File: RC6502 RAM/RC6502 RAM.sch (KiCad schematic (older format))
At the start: 23 parts, among them J3 RC6502_Backplane, U1 HM62256BLP-7, U2 74LS138, U3 74LS02, U4 74LS02, U5 74LS00

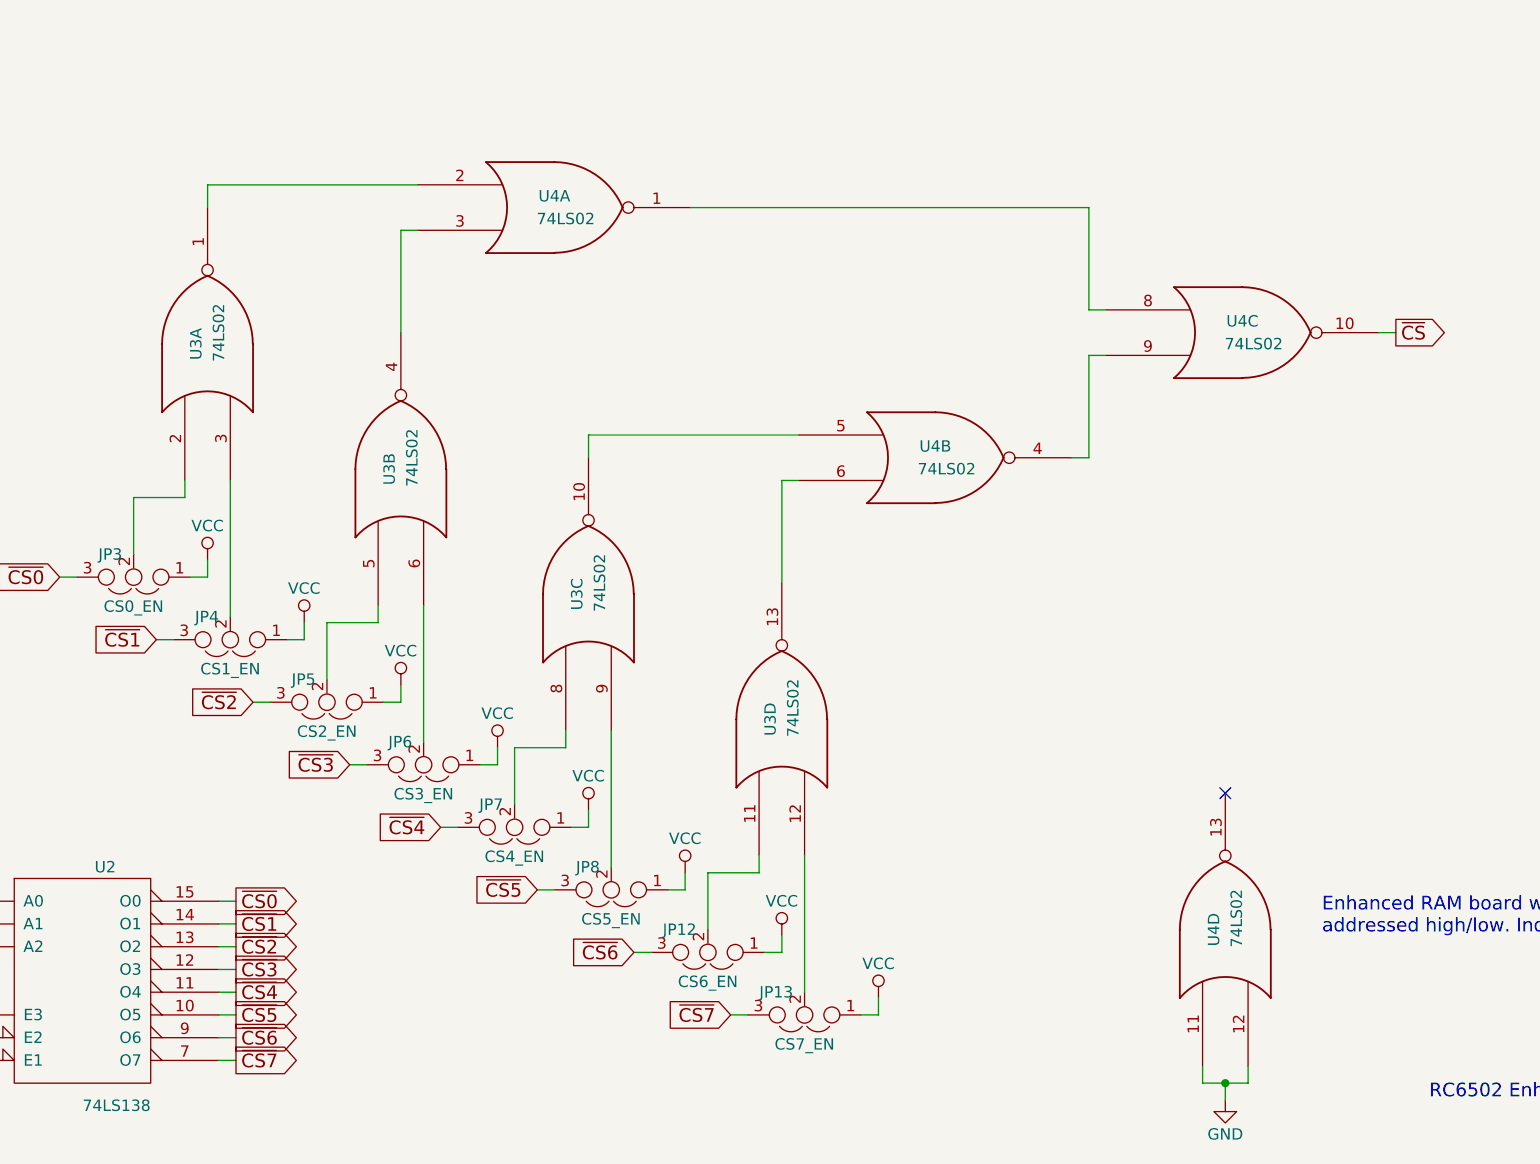
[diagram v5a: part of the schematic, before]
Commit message: Fixed RAM board block select logic
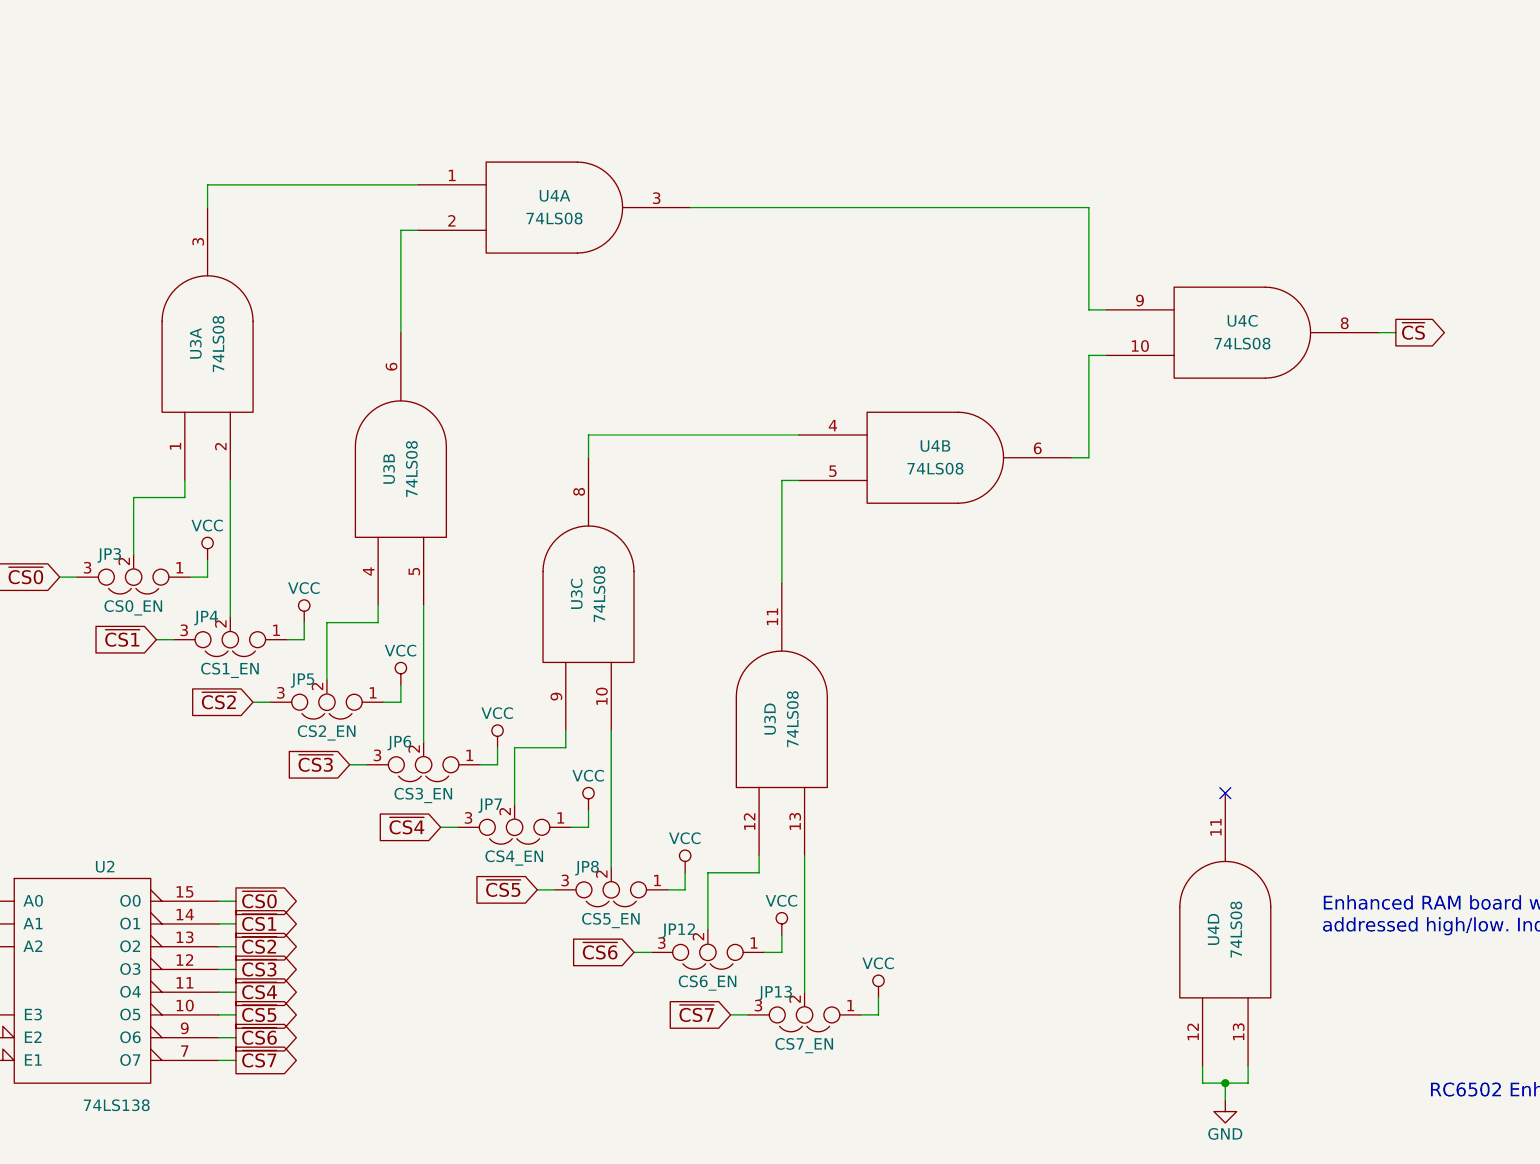
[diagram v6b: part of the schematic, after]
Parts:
- removed U3, U4: 74LS02, Housings_DIP:DIP-14_W7.62mm_Socket, symbol 74LS02
- added U3, U4: 74LS08, Housings_DIP:DIP-14_W7.62mm_Socket, symbol 74LS08
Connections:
- net GND: now also U3.7 (GND), U3.7 (GND), U3.7 (GND), U3.7 (GND), U4.12, U4.13, U4.7 (GND), U4.7 (GND), U4.7 (GND), U4.7 (GND)
- net VCC: now also U3.14 (VCC), U3.14 (VCC), U3.14 (VCC), U3.14 (VCC), U4.14 (VCC), U4.14 (VCC), U4.14 (VCC), U4.14 (VCC)
- net ~CS: now also U4.8
- net at JP3.2: now also U3.1
- net at JP4.2: now also U3.2
- net at JP5.2: now also U3.4
- net at JP6.2: now also U3.5
- net at JP7.2: now also U3.9
- net at JP8.2: now also U3.10
- net at JP12.2: now also U3.12
- net at JP13.2: now also U3.13
- new net: U3.3, U4.1
- new net: U3.6, U4.2
- new net: U3.8, U4.4
- new net: U3.11, U4.5
- new net: U4.3, U4.9
- new net: U4.10, U4.6
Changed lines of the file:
@@
 Wire Wire Line
 	2125 5125 2125 5200
-$Comp
-L 74LS02 U3
-U 1 1 5C1DAB94
-P 2125 4175
-F 0 "U3" H 2125 4225 50  0000 C CNN
-F 1 "74LS02" H 2175 4125 50  0000 C CNN
-F 2 "Housings_DIP:DIP-14_W7.62mm_Socket" H 2125 4175 50  0001 C CNN
-F 3 "" H 2125 4175 50  0001 C CNN
-	1    2125 4175
-	0    -1   -1   0
-$EndComp
 Wire Wire Line
 	1800 5100 1800 4850
@@
 Wire Wire Line
 	2975 5675 2975 5750
-$Comp
-L 74LS02 U3
-U 2 1 5C1DB812
-P 2975 4725
-F 0 "U3" H 2975 4775 50  0000 C CNN
-F 1 "74LS02" H 3025 4675 50  0000 C CNN
-F 2 "Housings_DIP:DIP-14_W7.62mm_Socket" H 2975 4725 50  0001 C CNN
-F 3 "" H 2975 4725 50  0001 C CNN
-	2    2975 4725
-	0    -1   -1   0
-$EndComp
 Wire Wire Line
 	2650 5650 2650 5400
@@
 Wire Wire Line
 	3800 6225 3800 6300
-$Comp
-L 74LS02 U3
-U 3 1 5C1DC564
-P 3800 5275
-F 0 "U3" H 3800 5325 50  0000 C CNN
-F 1 "74LS02" H 3850 5225 50  0000 C CNN
-F 2 "Housings_DIP:DIP-14_W7.62mm_Socket" H 3800 5275 50  0001 C CNN
-F 3 "" H 3800 5275 50  0001 C CNN
-	3    3800 5275
-	0    -1   -1   0
-$EndComp
 Wire Wire Line
 	3475 6200 3475 5950
@@
 Wire Wire Line
 	4650 6775 4650 6850
-$Comp
-L 74LS02 U3
-U 4 1 5C1DC58E
-P 4650 5825
-F 0 "U3" H 4650 5875 50  0000 C CNN
-F 1 "74LS02" H 4700 5775 50  0000 C CNN
-F 2 "Housings_DIP:DIP-14_W7.62mm_Socket" H 4650 5825 50  0001 C CNN
-F 3 "" H 4650 5825 50  0001 C CNN
-	4    4650 5825
-	0    -1   -1   0
-$EndComp
 Wire Wire Line
 	4325 6750 4325 6500
@@
 Wire Wire Line
 	4325 6500 4550 6500
-$Comp
-L 74LS02 U4
-U 1 1 5C1DE352
-P 3650 3575
-F 0 "U4" H 3650 3625 50  0000 C CNN
-F 1 "74LS02" H 3700 3525 50  0000 C CNN
-F 2 "Housings_DIP:DIP-14_W7.62mm_Socket" H 3650 3575 50  0001 C CNN
-F 3 "" H 3650 3575 50  0001 C CNN
-	1    3650 3575
-	1    0    0    -1
-$EndComp
 Wire Wire Line
 	2125 3475 2125 3575
@@
 Wire Wire Line
 	3050 3475 2125 3475
-$Comp
-L 74LS02 U4
-U 2 1 5C1DF2B7
-P 5325 4675
-F 0 "U4" H 5325 4725 50  0000 C CNN
-F 1 "74LS02" H 5375 4625 50  0000 C CNN
-F 2 "Housings_DIP:DIP-14_W7.62mm_Socket" H 5325 4675 50  0001 C CNN
-F 3 "" H 5325 4675 50  0001 C CNN
-	2    5325 4675
-	1    0    0    -1
-$EndComp
 Wire Wire Line
 	3800 4575 3800 4675
@@
 Wire Wire Line
 	4650 4775 4725 4775
-$Comp
-L 74LS02 U4
-U 3 1 5C1DFD68
-P 6675 4125
-F 0 "U4" H 6675 4175 50  0000 C CNN
-F 1 "74LS02" H 6725 4075 50  0000 C CNN
-F 2 "Housings_DIP:DIP-14_W7.62mm_Socket" H 6675 4125 50  0001 C CNN
-F 3 "" H 6675 4125 50  0001 C CNN
-	3    6675 4125
-	1    0    0    -1
-$EndComp
 Wire Wire Line
 	5925 4675 6000 4675
@@
 Connection ~ 10250 875
 Connection ~ 9650 875
-$Comp
-L 74LS02 U4
-U 4 1 5C1E36AB
-P 6600 6750
-F 0 "U4" H 6600 6800 50  0000 C CNN
-F 1 "74LS02" H 6650 6700 50  0000 C CNN
-F 2 "Housings_DIP:DIP-14_W7.62mm_Socket" H 6600 6750 50  0001 C CNN
-F 3 "" H 6600 6750 50  0001 C CNN
-	4    6600 6750
-	0    -1   -1   0
-$EndComp
 $Comp
 L GND #PWR015
@@
 Text Notes 7025 6775 0    60   ~ 0
 Enhanced RAM board with added support for ROM ICs of type 28C64 or 28C256, can be\naddressed high/low. Individual 4k blocks can be enabled via jumpers.
+$Comp
+L 74LS08 U3
+U 1 1 5C68602F
+P 2125 4175
+F 0 "U3" H 2125 4225 50  0000 C CNN
+F 1 "74LS08" H 2125 4125 50  0000 C CNN
+F 2 "Housings_DIP:DIP-14_W7.62mm_Socket" H 2125 4175 50  0001 C CNN
+F 3 "" H 2125 4175 50  0001 C CNN
+	1    2125 4175
+	0    -1   -1   0
+$EndComp
+$Comp
+L 74LS08 U3
+U 2 1 5C6865C4
+P 2975 4725
+F 0 "U3" H 2975 4775 50  0000 C CNN
+F 1 "74LS08" H 2975 4675 50  0000 C CNN
+F 2 "Housings_DIP:DIP-14_W7.62mm_Socket" H 2975 4725 50  0001 C CNN
+F 3 "" H 2975 4725 50  0001 C CNN
+	2    2975 4725
+	0    -1   -1   0
+$EndComp
+$Comp
+L 74LS08 U3
+U 3 1 5C686812
+P 3800 5275
+F 0 "U3" H 3800 5325 50  0000 C CNN
+F 1 "74LS08" H 3800 5225 50  0000 C CNN
+F 2 "Housings_DIP:DIP-14_W7.62mm_Socket" H 3800 5275 50  0001 C CNN
+F 3 "" H 3800 5275 50  0001 C CNN
+	3    3800 5275
+	0    -1   -1   0
+$EndComp
+$Comp
+L 74LS08 U3
+U 4 1 5C68689D
+P 4650 5825
+F 0 "U3" H 4650 5875 50  0000 C CNN
+F 1 "74LS08" H 4650 5775 50  0000 C CNN
+F 2 "Housings_DIP:DIP-14_W7.62mm_Socket" H 4650 5825 50  0001 C CNN
+F 3 "" H 4650 5825 50  0001 C CNN
+	4    4650 5825
+	0    -1   -1   0
+$EndComp
+$Comp
+L 74LS08 U4
+U 1 1 5C687BF2
+P 3650 3575
+F 0 "U4" H 3650 3625 50  0000 C CNN
+F 1 "74LS08" H 3650 3525 50  0000 C CNN
+F 2 "Housings_DIP:DIP-14_W7.62mm_Socket" H 3650 3575 50  0001 C CNN
+F 3 "" H 3650 3575 50  0001 C CNN
+	1    3650 3575
+	1    0    0    -1
+$EndComp
+$Comp
+L 74LS08 U4
+U 2 1 5C687CAF
+P 5325 4675
+F 0 "U4" H 5325 4725 50  0000 C CNN
+F 1 "74LS08" H 5325 4625 50  0000 C CNN
+F 2 "Housings_DIP:DIP-14_W7.62mm_Socket" H 5325 4675 50  0001 C CNN
+F 3 "" H 5325 4675 50  0001 C CNN
+	2    5325 4675
+	1    0    0    -1
+$EndComp
+$Comp
+L 74LS08 U4
+U 3 1 5C687D29
+P 6675 4125
+F 0 "U4" H 6675 4175 50  0000 C CNN
+F 1 "74LS08" H 6675 4075 50  0000 C CNN
+F 2 "Housings_DIP:DIP-14_W7.62mm_Socket" H 6675 4125 50  0001 C CNN
+F 3 "" H 6675 4125 50  0001 C CNN
+	3    6675 4125
+	1    0    0    -1
+$EndComp
+$Comp
+L 74LS08 U4
+U 4 1 5C687DB2
+P 6600 6750
+F 0 "U4" H 6600 6800 50  0000 C CNN
+F 1 "74LS08" H 6600 6700 50  0000 C CNN
+F 2 "Housings_DIP:DIP-14_W7.62mm_Socket" H 6600 6750 50  0001 C CNN
+F 3 "" H 6600 6750 50  0001 C CNN
+	4    6600 6750
+	0    -1   -1   0
+$EndComp
 $EndSCHEMATC
